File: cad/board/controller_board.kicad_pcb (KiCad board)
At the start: 2 copper layers, 75.6 x 73 mm, 13 parts, among them J1 Barrel_Jack, J2 Conn_01x12, J3 Conn_01x16, J4 Conn_01x12, U2 DIP-16-Socket

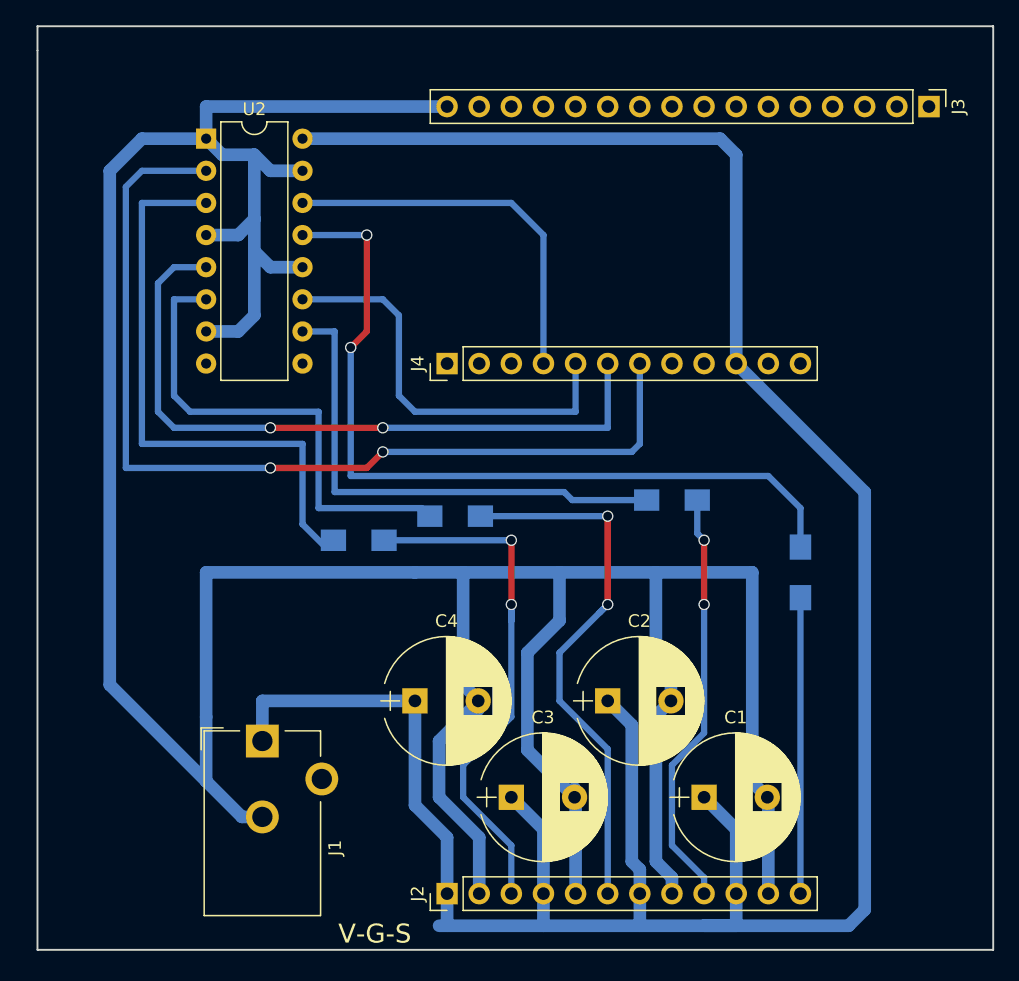
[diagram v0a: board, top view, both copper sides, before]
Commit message: re-design board with wider tracks, remove all unused copper with cam
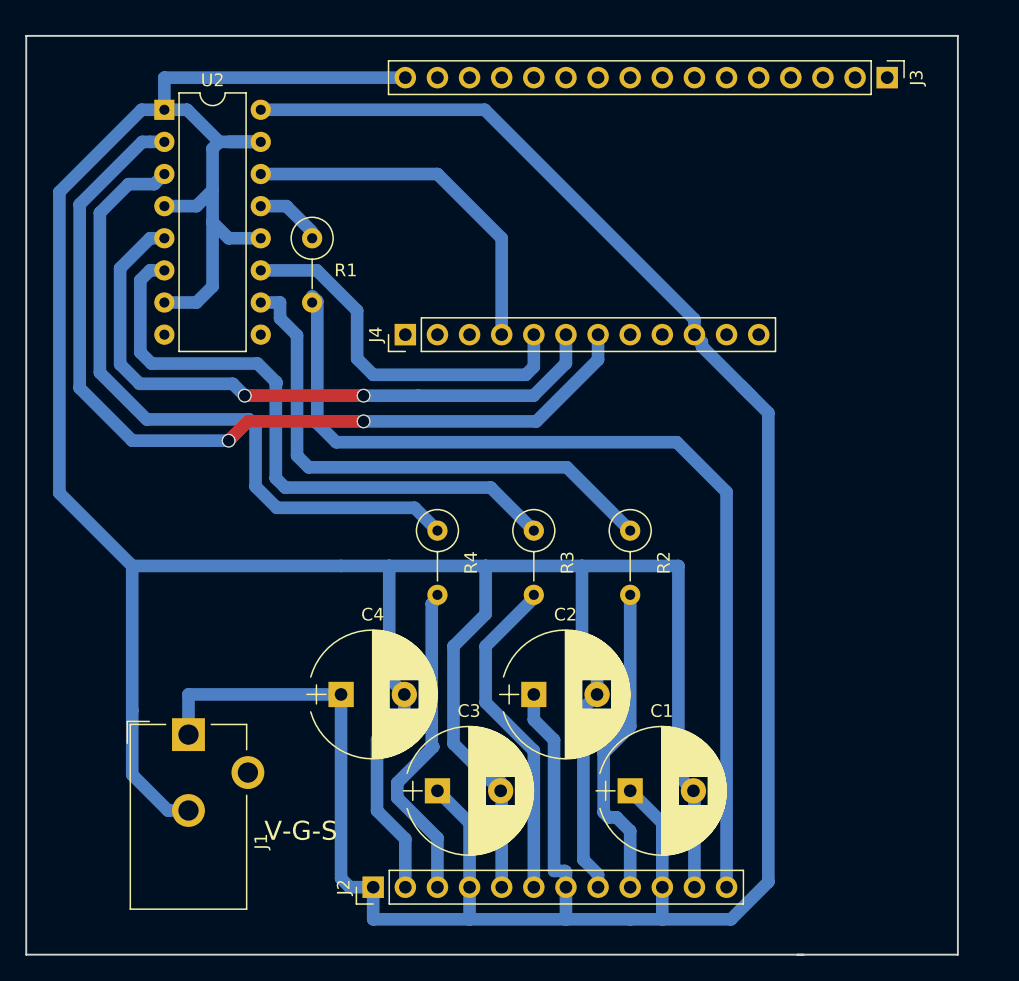
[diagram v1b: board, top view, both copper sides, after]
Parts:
- R1, R2, R3, R4: footprint Resistors_SMD:R_1206_HandSoldering -> Resistors_ThroughHole:R_Axial_DIN0309_L9.0mm_D3.2mm_P5.08mm_Vertical; moved to F.Cu
- moved R1 46.8 mm to (36.3, 29.5)
- moved R3 6.33 mm to (53.8, 52.6), turned to 270 degrees
- moved R4 6.27 mm to (46.2, 52.6), turned to 270 degrees
- moved C4 5.86 mm to (38.6, 65.5)
- moved C2 5.86 mm to (53.8, 65.5)
- moved J1 5.86 mm to (26.5, 68.7)
- moved C1 5.86 mm to (61.5, 73.2)
- moved C3 5.86 mm to (46.2, 73.2)
- moved J2 5.86 mm to (41.1, 80.8)
- moved R2 4.09 mm to (61.5, 52.6), turned to 270 degrees
- moved J3 4.02 mm to (81.8, 16.8)
- moved U2 4.02 mm to (24.6, 19.3)
- moved J4 4.02 mm to (43.7, 37.1)
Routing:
- net SH4: track 64.3 -> 4.91 mm, vias 2 -> 0
- net Net-(J2-Pad12): track 22.9 -> 76.1 mm
- net Net-(J2-Pad6): track 44.0 -> 26.0 mm, vias 2 -> 0
- net Net-(J2-Pad3): track 42.4 -> 25.6 mm, vias 2 -> 0
- net GND: track 293.1 -> 276.6 mm
- net VCC: track 210.8 -> 198.5 mm
- net SH2: track 38.8 -> 49.6 mm
- net SH1: track 45.7 -> 53.7 mm
- net Net-(J2-Pad9): track 33.4 -> 26.2 mm, vias 2 -> 0
- net SL1: track 76.9 -> 70.6 mm
- net SL2: track 55.7 -> 51.7 mm
- net SH3: track 40.2 -> 43.0 mm
- net SL3: track 32.8 -> 30.0 mm
- net SL4: track 30.3 -> 28.8 mm
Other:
- board size 75.6 x 73 mm -> 73.7 x 72.6 mm
- net class Default: clearance 0.4 -> 0.6; trace_width 0.5 -> 1; via_dia 0.9 -> 1.1; via_drill 0.7 -> 0.9
- net class Power: clearance 0.4 -> 0.6; via_dia 0.9 -> 1.1; via_drill 0.7 -> 0.9
- rule trace_clearance: 0.4 -> 0.6
